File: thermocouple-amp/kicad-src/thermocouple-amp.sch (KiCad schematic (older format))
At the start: 19 parts, among them J2 Conn_01x04, U2 AD8551RM

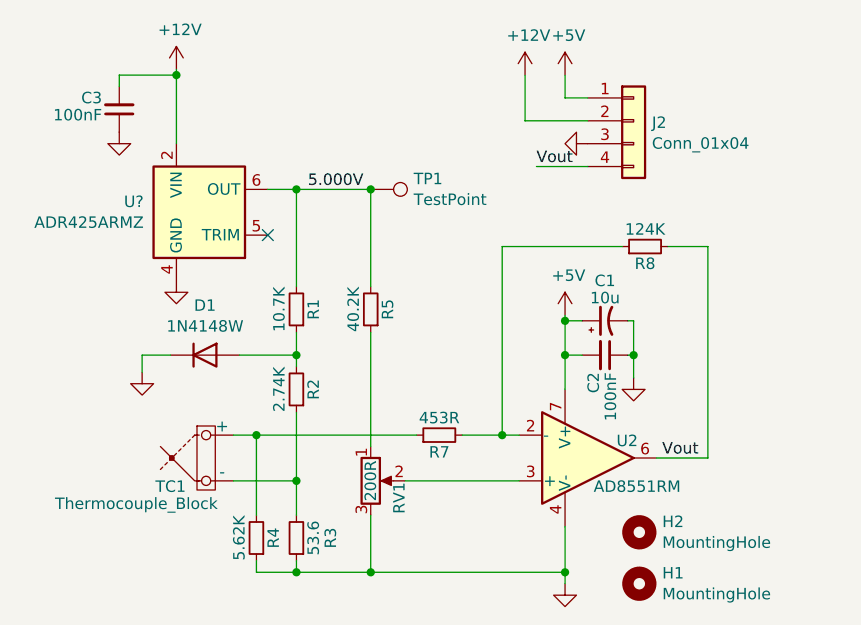
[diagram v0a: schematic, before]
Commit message: adds guard trace and prod files
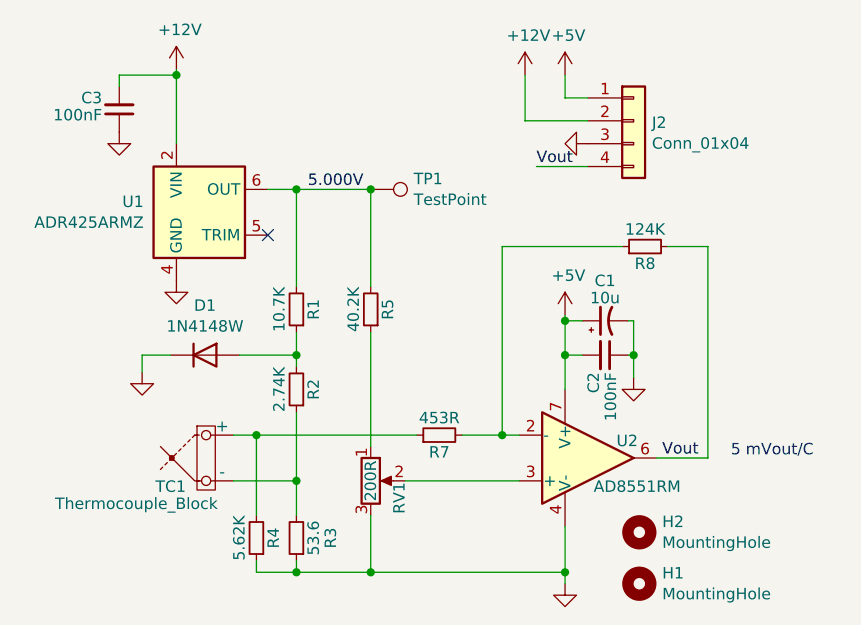
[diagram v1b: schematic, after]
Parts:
- gave numbers to parts that had none: 1
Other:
- note added: "5 mVout/C"
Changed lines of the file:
@@
 	5600 1900 5600 1700
 $Comp
-L Reference_Voltage:ADR425ARMZ U?
+L Reference_Voltage:ADR425ARMZ U1
 U 1 1 61BD40D0
 P 4175 2300
-F 0 "U?" H 3932 2346 50  0000 R CNN
+F 0 "U1" H 3932 2346 50  0000 R CNN
 F 1 "ADR425ARMZ" H 3932 2255 50  0000 R CNN
 F 2 "Package_SO:MSOP-8_3x3mm_P0.65mm" H 4175 1800 50  0001 C CNN
@@
 	1    0    0    -1
 $EndComp
+Text Notes 6500 3375 0    50   ~ 0
+5 mVout/C
 $EndSCHEMATC

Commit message: updates tc amp gerbers
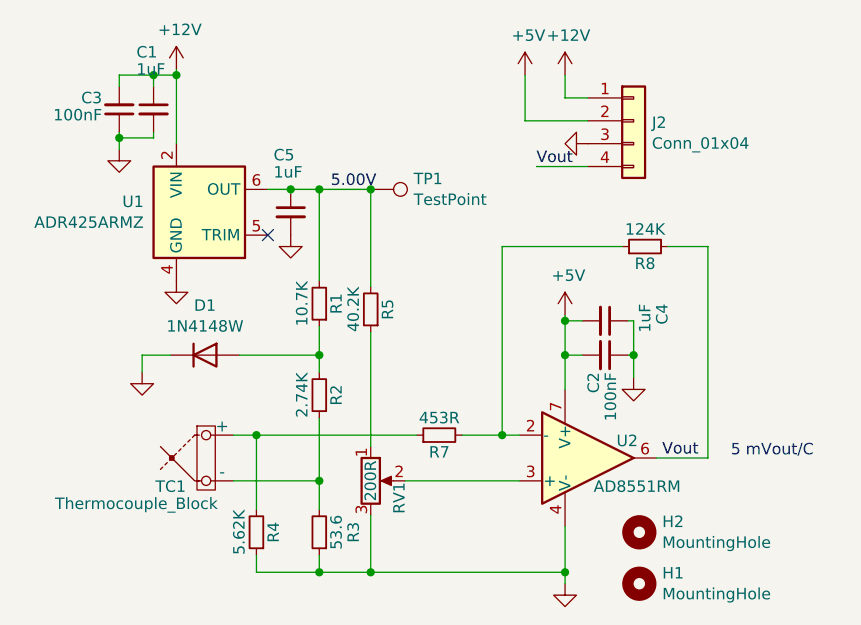
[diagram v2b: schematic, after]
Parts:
- removed C1: 10u, Capacitor_SMD:CP_Elec_3x5.4, symbol Device:CP1_Small
- added C1, C4, C5: 1uF, Capacitor_SMD:C_0603_1608Metric, symbol Device:C_Small
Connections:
- net +12V: now also J2.1 (Pin_1), C1.1; no longer J2.2 (Pin_2)
- net +5V: now also J2.2 (Pin_2), C4.2; no longer J2.1 (Pin_1)
- net GND: now also C1.2, C4.1, C5.2
- net 5.000V renamed 5.00V
- net 5.00V: now also C5.1
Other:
- moved on the sheet: R1, R2, R3, R4
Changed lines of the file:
@@
-$EndComp
-$Comp
-L Device:R_Small R1
-U 1 1 61AE9AB3
-P 4600 2725
-F 0 "R1" V 4525 2725 50  0000 C CNN
-F 1 "10.7K" V 4675 2725 50  0000 C CNN
-F 2 "Resistor_SMD:R_0603_1608Metric" H 4600 2725 50  0001 C CNN
-F 3 "~" H 4600 2725 50  0001 C CNN
-	1    4600 2725
-	-1   0    0    1
 $EndComp
 $Comp
@@
 $EndComp
 $Comp
-L Device:R_Small R2
-U 1 1 61AFBCD7
-P 4600 3075
-F 0 "R2" V 4525 3075 50  0000 C CNN
-F 1 "2.74K" V 4675 3075 50  0000 C CNN
-F 2 "Resistor_SMD:R_0603_1608Metric" H 4600 3075 50  0001 C CNN
-F 3 "~" H 4600 3075 50  0001 C CNN
-	1    4600 3075
-	-1   0    0    1
-$EndComp
-$Comp
 L Device:R_Small R3
 U 1 1 61AFC2B5
-P 4600 3725
-F 0 "R3" V 4450 3725 50  0000 C CNN
-F 1 "53.6" V 4525 3725 50  0000 C CNN
-F 2 "Resistor_SMD:R_0603_1608Metric" H 4600 3725 50  0001 C CNN
-F 3 "~" H 4600 3725 50  0001 C CNN
-	1    4600 3725
+P 4700 3700
+F 0 "R3" V 4550 3700 50  0000 C CNN
+F 1 "53.6" V 4625 3700 50  0000 C CNN
+F 2 "Resistor_SMD:R_0603_1608Metric" H 4700 3700 50  0001 C CNN
+F 3 "~" H 4700 3700 50  0001 C CNN
+	1    4700 3700
 	-1   0    0    1
 $EndComp
@@
 L Device:R_Small R4
 U 1 1 61B0AB8F
-P 4425 3725
-F 0 "R4" V 4350 3725 50  0000 C CNN
-F 1 "5.62K" V 4500 3725 50  0000 C CNN
-F 2 "Resistor_SMD:R_0603_1608Metric" H 4425 3725 50  0001 C CNN
-F 3 "~" H 4425 3725 50  0001 C CNN
-	1    4425 3725
+P 4425 3700
+F 0 "R4" V 4350 3700 50  0000 C CNN
+F 1 "5.62K" V 4500 3700 50  0000 C CNN
+F 2 "Resistor_SMD:R_0603_1608Metric" H 4425 3700 50  0001 C CNN
+F 3 "~" H 4425 3700 50  0001 C CNN
+	1    4425 3700
 	-1   0    0    1
 $EndComp
@@
 $EndComp
 $Comp
-L Device:CP1_Small C1
-U 1 1 61B506BF
-P 5950 2775
-F 0 "C1" V 6125 2775 50  0000 C CNN
-F 1 "10u" V 6050 2775 50  0000 C CNN
-F 2 "Capacitor_SMD:CP_Elec_3x5.4" H 5950 2775 50  0001 C CNN
-F 3 "~" H 5950 2775 50  0001 C CNN
-	1    5950 2775
-	0    -1   -1   0
-$EndComp
-$Comp
 L power:GND #PWR010
 U 1 1 61B6C07A
@@
 L power:GND #PWR01
 U 1 1 61B73DAB
-P 3825 1950
-F 0 "#PWR01" H 3825 1700 50  0001 C CNN
-F 1 "GND" H 3830 1777 50  0001 C CNN
-F 2 "" H 3825 1950 50  0001 C CNN
-F 3 "" H 3825 1950 50  0001 C CNN
-	1    3825 1950
+P 3825 2025
+F 0 "#PWR01" H 3825 1775 50  0001 C CNN
+F 1 "GND" H 3830 1852 50  0001 C CNN
+F 2 "" H 3825 2025 50  0001 C CNN
+F 3 "" H 3825 2025 50  0001 C CNN
+	1    3825 2025
 	1    0    0    -1
 $EndComp
@@
 	3825 1750 3825 1700
 Wire Wire Line
-	3825 1700 4075 1700
+	3825 1700 3975 1700
 Wire Wire Line
 	4075 1700 4075 1675
@@
 	4925 3325 4925 2825
 Wire Wire Line
-	4925 2200 4600 2200
-Wire Wire Line
 	4925 2200 4925 2625
 Wire Wire Line
-	4600 2625 4600 2200
-Connection ~ 4600 2200
-Wire Wire Line
-	4600 2200 4475 2200
-Wire Wire Line
-	4600 2825 4600 2925
-Wire Wire Line
-	4350 2925 4600 2925
-Connection ~ 4600 2925
-Wire Wire Line
-	4600 2925 4600 2975
-Wire Wire Line
-	4600 3175 4600 3475
+	4700 2600 4700 2200
+Connection ~ 4700 2200
+Wire Wire Line
+	4700 2200 4575 2200
+Wire Wire Line
+	4700 2800 4700 2925
+Wire Wire Line
+	4350 2925 4700 2925
+Connection ~ 4700 2925
+Wire Wire Line
+	4700 2925 4700 3000
+Wire Wire Line
+	4700 3200 4700 3475
 Wire Wire Line
 	5775 3675 5775 3875
@@
 	5775 3875 4925 3875
 Wire Wire Line
-	4600 3875 4600 3825
+	4700 3875 4700 3800
 Connection ~ 5775 3875
 Wire Wire Line
 	5775 3875 5775 3925
 Wire Wire Line
-	4600 3875 4425 3875
-Wire Wire Line
-	4425 3875 4425 3825
-Connection ~ 4600 3875
-Wire Wire Line
-	4600 3475 4325 3475
-Connection ~ 4600 3475
-Wire Wire Line
-	4600 3475 4600 3625
-Wire Wire Line
-	4425 3625 4425 3275
+	4700 3875 4425 3875
+Wire Wire Line
+	4425 3875 4425 3800
+Connection ~ 4700 3875
+Wire Wire Line
+	4700 3475 4325 3475
+Connection ~ 4700 3475
+Wire Wire Line
+	4700 3475 4700 3600
+Wire Wire Line
+	4425 3600 4425 3275
 Connection ~ 4425 3275
 Wire Wire Line
@@
 Connection ~ 4925 3875
 Wire Wire Line
-	4925 3875 4600 3875
-Text Label 4650 2200 0    50   ~ 0
-5.000V
+	4925 3875 4700 3875
+Text Label 4750 2200 0    50   ~ 0
+5.00V
 Text Label 6200 3375 0    50   ~ 0
 Vout
@@
 L power:+5V #PWR06
 U 1 1 61BBA30B
-P 5775 1700
-F 0 "#PWR06" H 5775 1550 50  0001 C CNN
-F 1 "+5V" H 5790 1873 50  0000 C CNN
-F 2 "" H 5775 1700 50  0001 C CNN
-F 3 "" H 5775 1700 50  0001 C CNN
-	1    5775 1700
+P 5600 1700
+F 0 "#PWR06" H 5600 1550 50  0001 C CNN
+F 1 "+5V" H 5615 1873 50  0000 C CNN
+F 2 "" H 5600 1700 50  0001 C CNN
+F 3 "" H 5600 1700 50  0001 C CNN
+	1    5600 1700
 	1    0    0    -1
 $EndComp
@@
 L power:+12V #PWR05
 U 1 1 61BCB7D4
-P 5600 1700
-F 0 "#PWR05" H 5600 1550 50  0001 C CNN
-F 1 "+12V" H 5615 1873 50  0000 C CNN
-F 2 "" H 5600 1700 50  0001 C CNN
-F 3 "" H 5600 1700 50  0001 C CNN
-	1    5600 1700
+P 5775 1700
+F 0 "#PWR05" H 5775 1550 50  0001 C CNN
+F 1 "+12V" H 5790 1873 50  0000 C CNN
+F 2 "" H 5775 1700 50  0001 C CNN
+F 3 "" H 5775 1700 50  0001 C CNN
+	1    5775 1700
 	1    0    0    -1
 $EndComp
@@
 Text Notes 6500 3375 0    50   ~ 0
 5 mVout/C
+$Comp
+L Device:C_Small C5
+U 1 1 61C21658
+P 4575 2300
+F 0 "C5" H 4500 2550 50  0000 L CNN
+F 1 "1uF" H 4500 2475 50  0000 L CNN
+F 2 "Capacitor_SMD:C_0603_1608Metric" H 4575 2300 50  0001 C CNN
+F 3 "~" H 4575 2300 50  0001 C CNN
+	1    4575 2300
+	1    0    0    -1
+$EndComp
+$Comp
+L power:GND #PWR011
+U 1 1 61C23D5A
+P 4575 2400
+F 0 "#PWR011" H 4575 2150 50  0001 C CNN
+F 1 "GND" H 4580 2227 50  0001 C CNN
+F 2 "" H 4575 2400 50  0001 C CNN
+F 3 "" H 4575 2400 50  0001 C CNN
+	1    4575 2400
+	1    0    0    -1
+$EndComp
+$Comp
+L Device:R_Small R2
+U 1 1 61AFBCD7
+P 4700 3100
+F 0 "R2" V 4625 3100 50  0000 C CNN
+F 1 "2.74K" V 4775 3100 50  0000 C CNN
+F 2 "Resistor_SMD:R_0603_1608Metric" H 4700 3100 50  0001 C CNN
+F 3 "~" H 4700 3100 50  0001 C CNN
+	1    4700 3100
+	-1   0    0    1
+$EndComp
+$Comp
+L Device:R_Small R1
+U 1 1 61AE9AB3
+P 4700 2700
+F 0 "R1" V 4625 2700 50  0000 C CNN
+F 1 "10.7K" V 4775 2700 50  0000 C CNN
+F 2 "Resistor_SMD:R_0603_1608Metric" H 4700 2700 50  0001 C CNN
+F 3 "~" H 4700 2700 50  0001 C CNN
+	1    4700 2700
+	-1   0    0    1
+$EndComp
+Wire Wire Line
+	4700 2200 4925 2200
+Connection ~ 4575 2200
+Wire Wire Line
+	4575 2200 4475 2200
+Wire Wire Line
+	3975 1700 3975 1750
+Connection ~ 3975 1700
+Wire Wire Line
+	3975 1700 4075 1700
+Wire Wire Line
+	3975 1950 3975 1975
+Wire Wire Line
+	3975 1975 3825 1975
+Wire Wire Line
+	3825 1975 3825 1950
+Connection ~ 3825 1975
+Wire Wire Line
+	3825 1975 3825 2025
+$Comp
+L Device:C_Small C1
+U 1 1 61C73F2E
+P 3975 1850
+F 0 "C1" H 3900 2100 50  0000 L CNN
+F 1 "1uF" H 3900 2025 50  0000 L CNN
+F 2 "Capacitor_SMD:C_0603_1608Metric" H 3975 1850 50  0001 C CNN
+F 3 "~" H 3975 1850 50  0001 C CNN
+	1    3975 1850
+	1    0    0    -1
+$EndComp
+$Comp
+L Device:C_Small C4
+U 1 1 61C7449E
+P 5950 2775
+F 0 "C4" H 5875 3025 50  0000 L CNN
+F 1 "1uF" H 5875 2950 50  0000 L CNN
+F 2 "Capacitor_SMD:C_0603_1608Metric" H 5950 2775 50  0001 C CNN
+F 3 "~" H 5950 2775 50  0001 C CNN
+	1    5950 2775
+	0    1    1    0
+$EndComp
 $EndSCHEMATC
